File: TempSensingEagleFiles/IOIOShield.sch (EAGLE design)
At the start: 3 parts

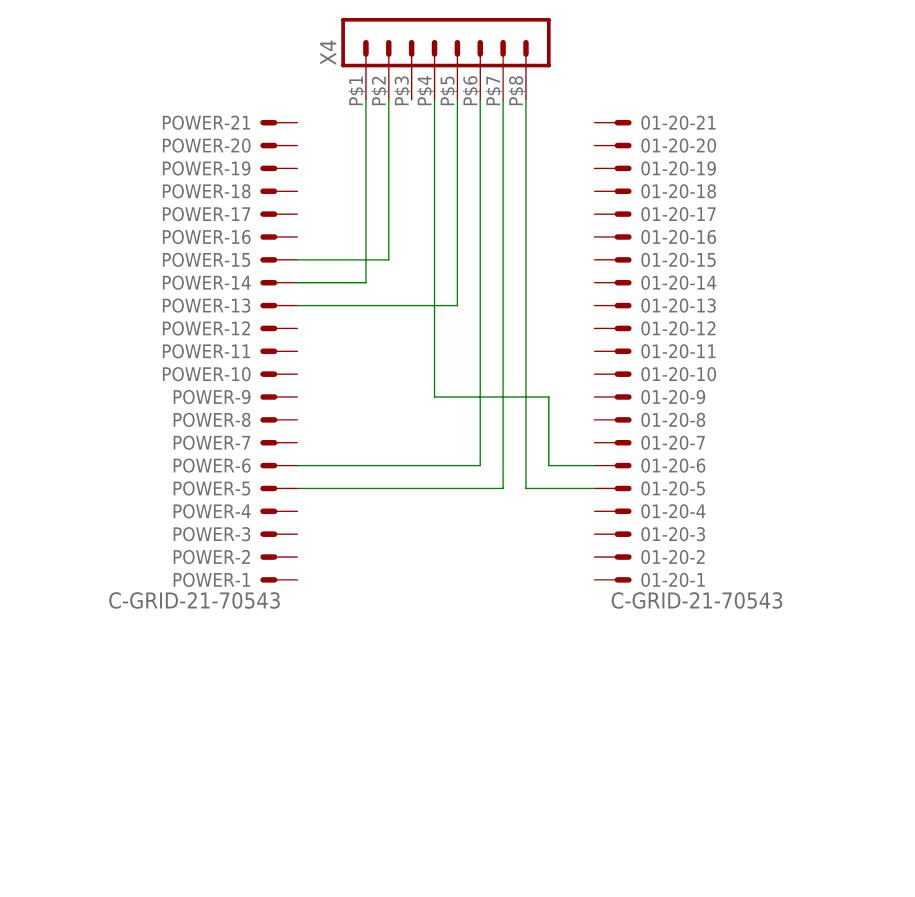
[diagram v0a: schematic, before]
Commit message: STABLE: working with only one sensor
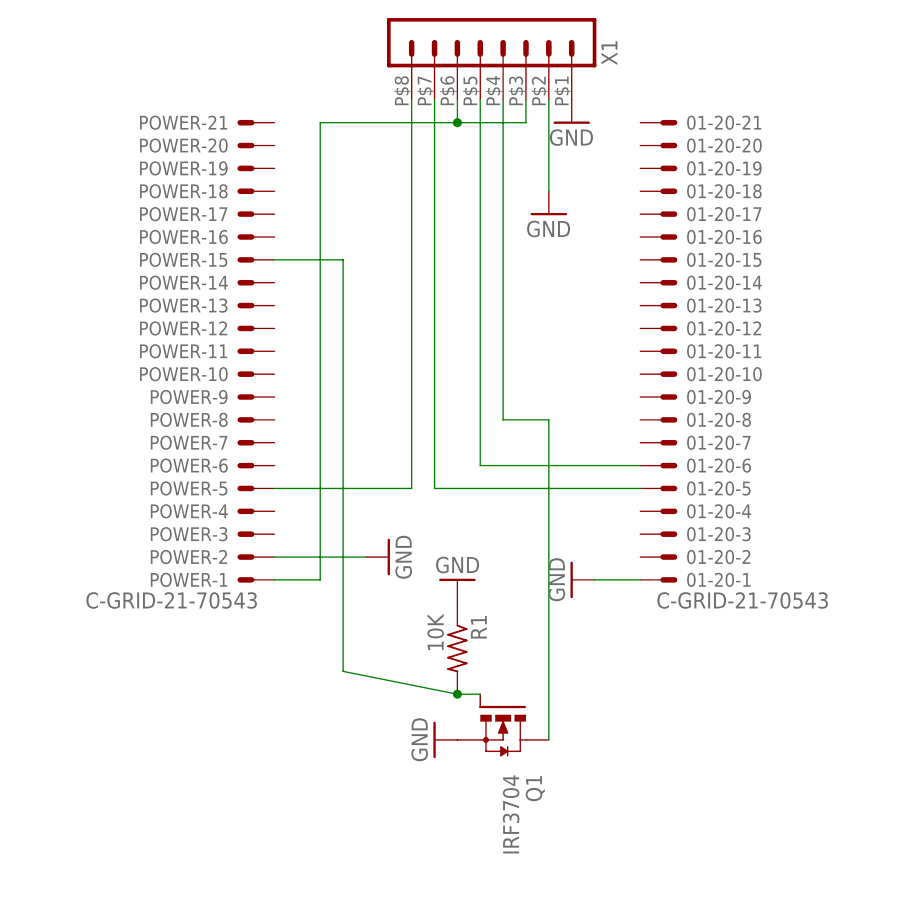
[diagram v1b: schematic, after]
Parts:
- removed X4: (no value), con-molex-micro-fit-3_0:HEADER_POS8_43045-0800
- added Q1: IRF3704, transistor-power:IRF3704
- added R1: 10K, rcl:R-US_0204/7
- added X1: (no value), con-molex-micro-fit-3_0:HEADER_POS8_43045-0800
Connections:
- removed net N$4: POWER-6.S, X4.6
- new net GND: 01-20-1.S, POWER-2.S, Q1.S, R1.1, X1.1, X1.2
- net N$1: now also Q1.G, R1.2; no longer X4.2
- net N$2: now also Q1.D, X1.4; no longer POWER-14.S, X4.1
- net N$3: now also POWER-1.S, X1.3, X1.6; no longer POWER-13.S, X4.5
- net N$5: now also X1.8; no longer X4.7
- net N$6: now also X1.5; no longer X4.4
- net N$8: now also X1.7; no longer X4.8
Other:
- moved on the sheet: 01-20-1, 01-20-10, 01-20-11, 01-20-12, 01-20-13, 01-20-14, 01-20-15, 01-20-16, 01-20-17, 01-20-18, 01-20-19, 01-20-2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
